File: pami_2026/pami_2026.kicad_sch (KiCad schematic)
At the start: 0 parts

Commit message: WIP actuators
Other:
- added sheet Actuators, Sensors, Utility (asu.kicad_sch)
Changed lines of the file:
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@@
+	)
+	(sheet
+		(at 142.24 91.44)
+		(size 29.21 20.32)
+		(exclude_from_sim no)
+		(in_bom yes)
+		(on_board yes)
+		(dnp no)
+		(fields_autoplaced yes)
+		(stroke
+			(width 0.1524)
+			(type solid)
+		)
+		(fill
+			(color 0 0 0 0.0000)
+		)
+		(property "Sheetname" "Actuators, Sensors, Utility"
+			(at 142.24 90.7284 0)
+			(effects
+				(font
+					(size 1.27 1.27)
+				)
+				(justify left bottom)
+			)
+		)
+		(property "Sheetfile" "asu.kicad_sch"
+			(at 142.24 112.3446 0)
+			(effects
+				(font
+					(size 1.27 1.27)
+				)
+				(justify left top)
+			)
+		)
+		(instances
+			(project "pami_2026"
+				(path "/2e16a05b-e8ca-4fff-9c3e-5c880745daa6"
+					(page "4")
+				)
+			)
+		)
 	)
 	(sheet

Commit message: FEAT : Routing
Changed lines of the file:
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@@
 	(paper "A4")
 	(sheet
-		(at 115.57 60.96)
+		(at 114.3 50.8)
 		(size 25.4 21.59)
 		(exclude_from_sim no)
@@
 		)
 		(property "Sheetname" "Microcontroller"
-			(at 115.57 60.2484 0)
+			(at 114.3 50.0884 0)
 			(effects
 				(font
@@
 		)
 		(property "Sheetfile" "Microcontroller.kicad_sch"
-			(at 115.57 83.1346 0)
+			(at 114.3 72.9746 0)
 			(effects
 				(font
@@
 	)
 	(sheet
-		(at 142.24 91.44)
-		(size 29.21 20.32)
+		(at 152.4 50.8)
+		(size 25.4 21.59)
 		(exclude_from_sim no)
 		(in_bom yes)
@@
 		)
 		(property "Sheetname" "Actuators, Sensors, Utility"
-			(at 142.24 90.7284 0)
+			(at 152.4 50.0884 0)
 			(effects
 				(font
@@
 		)
 		(property "Sheetfile" "asu.kicad_sch"
-			(at 142.24 112.3446 0)
+			(at 152.4 72.9746 0)
 			(effects
 				(font
@@
 	)
 	(sheet
-		(at 156.21 59.69)
-		(size 22.86 19.05)
+		(at 76.2 50.8)
+		(size 25.4 21.59)
 		(exclude_from_sim no)
 		(in_bom yes)
@@
 		)
 		(property "Sheetname" "Power"
-			(at 156.21 58.9784 0)
+			(at 76.2 50.0884 0)
 			(effects
 				(font
@@
 		)
 		(property "Sheetfile" "Power.kicad_sch"
-			(at 156.21 79.3246 0)
+			(at 76.2 72.9746 0)
 			(effects
 				(font

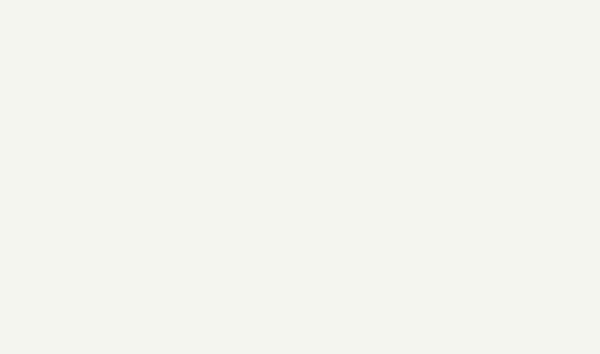
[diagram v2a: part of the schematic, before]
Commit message: Feat: mounting holes, indications, fix capa polarity
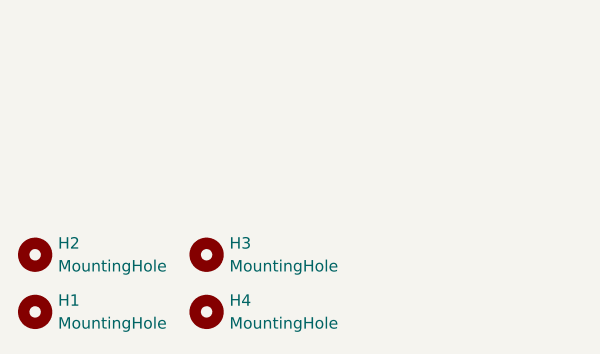
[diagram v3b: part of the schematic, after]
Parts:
- added H1, H2, H3, H4: MountingHole, MountingHole:MountingHole_2.2mm_M2_ISO7380_Pad, symbol Mechanical:MountingHole

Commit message: Cleanup
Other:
- sheet Actuators, Sensors, Utility ports: added DC_A1, DC_A2, DC_B1, DC_B2, HALL_A1, HALL_A2, HALL_B1, HALL_B2; removed none
- sheet Microcontroller ports: added BATTERY_LEVEL, DC_A1, DC_A2, DC_B1, DC_B2, HALL_A1, HALL_A2, HALL_B1, HALL_B2; removed none
- sheet Power ports: added BATTERY_LEVEL; removed none
